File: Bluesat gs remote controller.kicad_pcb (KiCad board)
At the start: 2 copper layers, 89.4 x 101.8 mm, 73 parts, among them J1 USB_C_Receptacle_USB2.0_16P, J2 Conn_01x02, J3 Conn_01x04, J4 Conn_01x04, J5 Conn_01x06, J6 Conn_01x02, Q1 Q_PMOS_GSD, SW1 Reset, SW2 Boot, SW3 AZ, SW4 EL, SW5 SW_SPDT, SW6 SW_Push, SW7 SW_Push, SW8 SW_Push, SW9 SW_Push, U1 MCP73831-2-OT, U2 SY8089AAAC, U4 ESP32-S3-WROOM-1

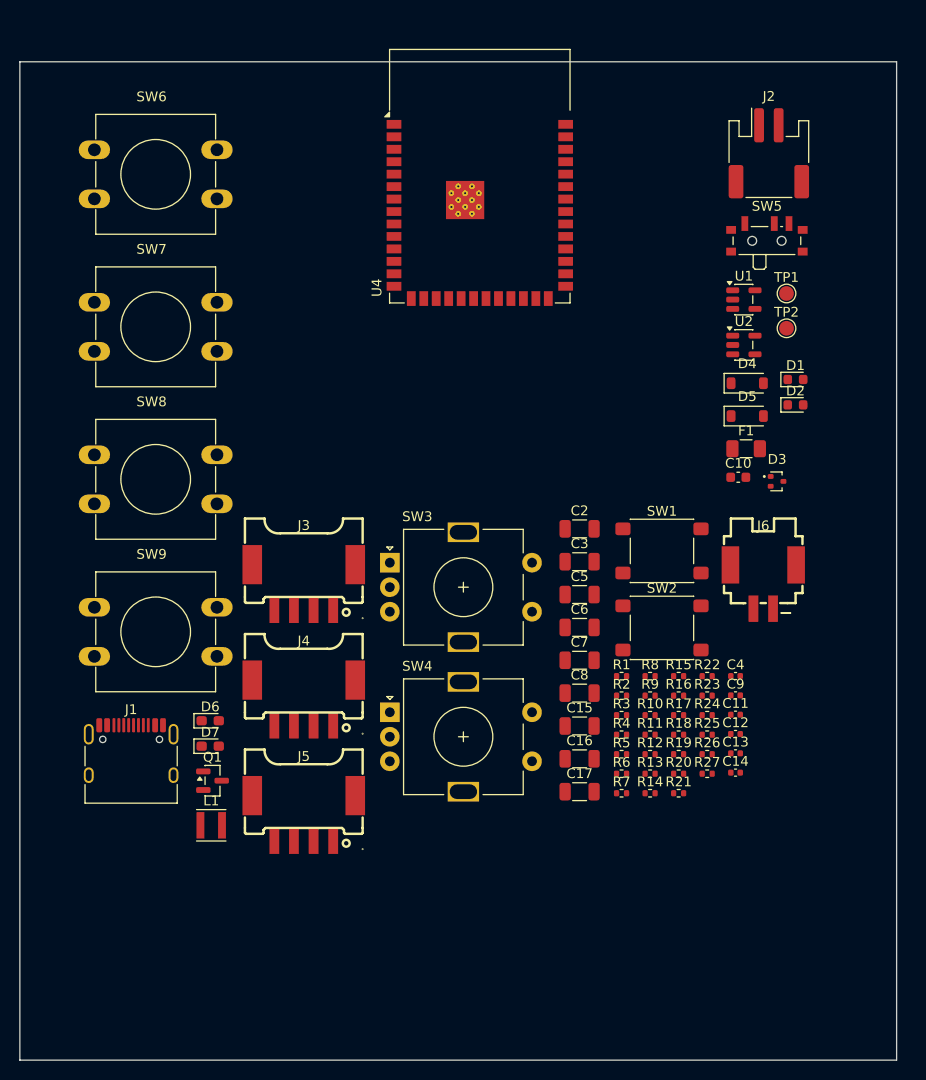
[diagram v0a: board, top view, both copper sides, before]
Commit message: Rotator remote: placement done, pre-routing review
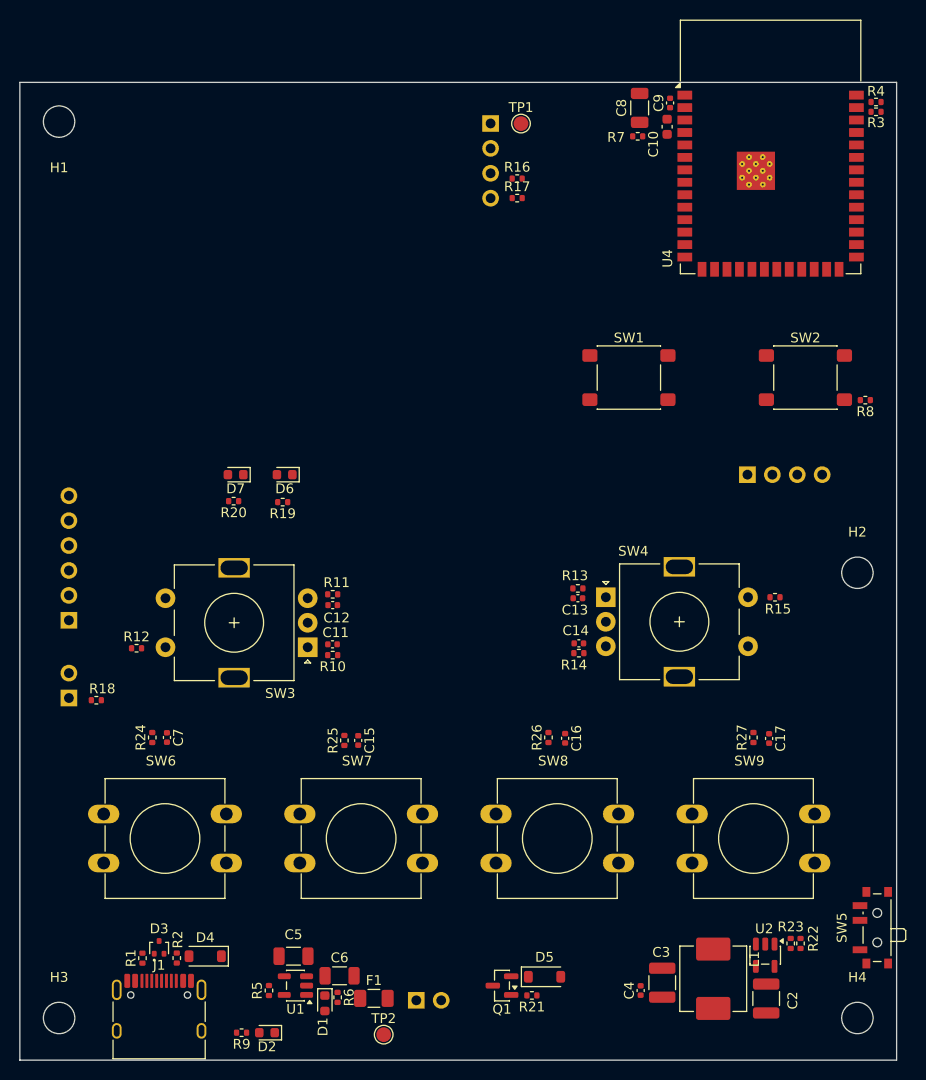
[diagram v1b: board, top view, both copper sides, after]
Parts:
- added H1: MountingHole_3.2mm_M3, MountingHole:MountingHole_3.2mm_M3, F.Cu at (105.2, 53.9)
- added H2: MountingHole_3.2mm_M3, MountingHole:MountingHole_3.2mm_M3, F.Cu at (186.6, 99.9)
- added H3: MountingHole_3.2mm_M3, MountingHole:MountingHole_3.2mm_M3, F.Cu at (105.2, 145.3)
- added H4: MountingHole_3.2mm_M3, MountingHole:MountingHole_3.2mm_M3, F.Cu at (186.6, 145.3)
- C15, C16, C17, C7: footprint Capacitor_SMD:C_1206_3216Metric -> Capacitor_SMD:C_0402_1005Metric
- C2, C3: footprint Capacitor_SMD:C_1206_3216Metric -> Capacitor_SMD:C_1210_3225Metric
- D6, D7: footprint LED_SMD:LED_0603_1608Metric_Pad1.05x0.95mm_HandSolder -> LED_SMD:LED_0603_1608Metric
- J2: footprint Connector_JST:JST_PH_S2B-PH-SM4-TB_1x02-1MP_P2.00mm_Horizontal -> Connector_PinHeader_2.54mm:PinHeader_1x02_P2.54mm_Vertical; moved to B.Cu
- J3, J4: footprint easyeda2kicad:CONN-SMD_SM04B-PASS-TBT-LF-SN -> Connector_PinHeader_2.54mm:PinHeader_1x04_P2.54mm_Vertical; moved to B.Cu
- J5: footprint easyeda2kicad:CONN-SMD_SM04B-PASS-TBT-LF-SN -> Connector_PinHeader_2.54mm:PinHeader_1x06_P2.54mm_Vertical; moved to B.Cu
- J6: footprint easyeda2kicad:CONN-TH_HX-SM02B-PASS-TB -> Connector_PinHeader_2.54mm:PinHeader_1x02_P2.54mm_Vertical; moved to B.Cu
- L1: value L -> 2.2uH; footprint Inductor_SMD:L_Taiyo-Yuden_NR-30xx -> Inductor_SMD:L_Changjiang_FXL0630
- R16, R17: value 4.7k -> 4k7
- R6: value 470Ω -> 470R
- moved J2 93.6 mm to (141.6, 143.5), turned to -90 degrees
- moved D2 83.7 mm to (126.4, 146.8), turned to 180 degrees
- moved U1 83.6 mm to (129.3, 142.0), turned to 180 degrees
- moved TP2 82.9 mm to (138.3, 147.0)
- moved D4 80.4 mm to (120.1, 139.0), turned to 180 degrees
- moved D1 79.7 mm to (132.3, 143.8), turned to -90 degrees
- moved D3 78.9 mm to (115.4, 138.1), turned to 90 degrees
- moved J6 71.7 mm to (106.2, 112.7)
- moved SW5 71.2 mm to (188.3, 136.1), turned to 90 degrees
- moved R4 69.5 mm to (188.5, 51.9)
- moved SW6 67.7 mm to (109.8, 124.5)
- moved F1 67.7 mm to (137.3, 143.3)
- moved R7 67.0 mm to (164.2, 55.4)
- moved R3 66.8 mm to (188.5, 52.9), turned to 180 degrees
- moved SW9 64.5 mm to (169.8, 124.5)
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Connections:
- C12 pad 1: GND -> /ENC_AZ_B
- C12 pad 2: /ENC_AZ_B -> GND
- C13 pad 2: Net-(C13-Pad2) -> GND
- C14 pad 1: Net-(C13-Pad2) -> /ENC_EL_B
- C14 pad 2: /ENC_EL_B -> GND
- C3 pad 2: /+3V3 -> +3.3V
- C4 pad 1: /+3V3 -> +3.3V
- C5 pad 2: /5V -> +5V
- C8 pad 1: /+3V3 -> +3.3V
- C9 pad 1: /+3V3 -> +3.3V
- D4 pad 1: /5V -> +5V
- D5 pad 2: /5V -> +5V
- J3 pad 1: unconnected-(J3-Pin_1-Pad1) -> +3.3V
- J4 pad 1: /+3V3 -> +3.3V
- J5 pad 1: /+3V3 -> +3.3V
- L1 pad 2: /+3V3 -> +3.3V
- Q1 pad 1: /5V -> +5V
- R10 pad 1: /+3V3 -> +3.3V
- R11 pad 1: /+3V3 -> +3.3V
- R12 pad 1: /+3V3 -> +3.3V
- R13 pad 1: /+3V3 -> +3.3V
- R14 pad 1: /+3V3 -> +3.3V
- R15 pad 1: /+3V3 -> +3.3V
- R16 pad 2: /+3V3 -> +3.3V
- R17 pad 2: /+3V3 -> +3.3V
- R18 pad 1: /+3V3 -> +3.3V
- R21 pad 2: /5V -> +5V
- R22 pad 2: /+3V3 -> +3.3V
- R24 pad 2: /+3V3 -> +3.3V
- R25 pad 2: /+3V3 -> +3.3V
- R26 pad 2: /+3V3 -> +3.3V
- R27 pad 2: /+3V3 -> +3.3V
- R5 pad 1: /5V -> GND
- R6 pad 1: /5V -> +5V
- R7 pad 1: /+3V3 -> +3.3V
- R8 pad 1: /+3V3 -> +3.3V
- R9 pad 2: /5V -> +5V
- SW2 pad 1: Net-(U4-IO0) -> GND
- SW2 pad 2: GND -> Net-(U4-IO0)
- SW5 pad 1: /VSYS -> /VPATH
- SW5 pad 2: /VPATH -> /VSYS
- TP1 pad 1: /+3V3 -> +3.3V
- U1 pad 4: /5V -> +5V
- U4 pad 2: /+3V3 -> +3.3V
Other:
- board size 89.4 x 101.8 mm -> 89.4 x 99.7 mm
